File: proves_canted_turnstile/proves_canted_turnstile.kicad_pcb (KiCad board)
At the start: 2 copper layers, 11.2 x 10 mm, 17 parts, among them J1 Conn_Coaxial, U1 QBA-07+, U2 QBA-07+, U3 QBA-07+

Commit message: updates
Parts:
- UHF 180: renamed from UHF 0
- UHF 270: renamed from UHF 0
- UHF 90: renamed from UHF 0
- moved UHF 0 71.6 mm to (69.1, 108.8)
- moved UHF 180 71.6 mm to (62.4, 149.7)
- moved UHF 270 71.6 mm to (85.6, 131.4)
- moved UHF 90 71.6 mm to (30.9, 138.2)
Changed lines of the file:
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@@
 	(footprint "Turnstile_Library:Singular_Tape_Measure_Antenna"
 		(layer "F.Cu")
-		(at 121.746067 109.720487 50)
-		(property "Reference" "UHF 0"
+		(at 62.357 149.733 50)
+		(property "Reference" "UHF 180"
 			(at -4.967884 1.59847 0)
 			(unlocked yes)
@@
 	(footprint "Turnstile_Library:Singular_Tape_Measure_Antenna"
 		(layer "F.Cu")
-		(at 90.250067 98.163487 50)
-		(property "Reference" "UHF 0"
+		(at 30.861 138.176 50)
+		(property "Reference" "UHF 90"
 			(at -4.967884 1.59847 0)
 			(unlocked yes)
@@
 	(footprint "Turnstile_Library:Singular_Tape_Measure_Antenna"
 		(layer "F.Cu")
-		(at 144.987067 91.432487 50)
-		(property "Reference" "UHF 0"
+		(at 85.598 131.445 50)
+		(property "Reference" "UHF 270"
 			(at -4.967884 1.59847 0)
 			(unlocked yes)
@@
 	(footprint "Turnstile_Library:Singular_Tape_Measure_Antenna"
 		(layer "F.Cu")
-		(at 128.477067 68.826487 50)
+		(at 69.088 108.839 50)
 		(property "Reference" "UHF 0"
 			(at -4.967884 1.59847 0)

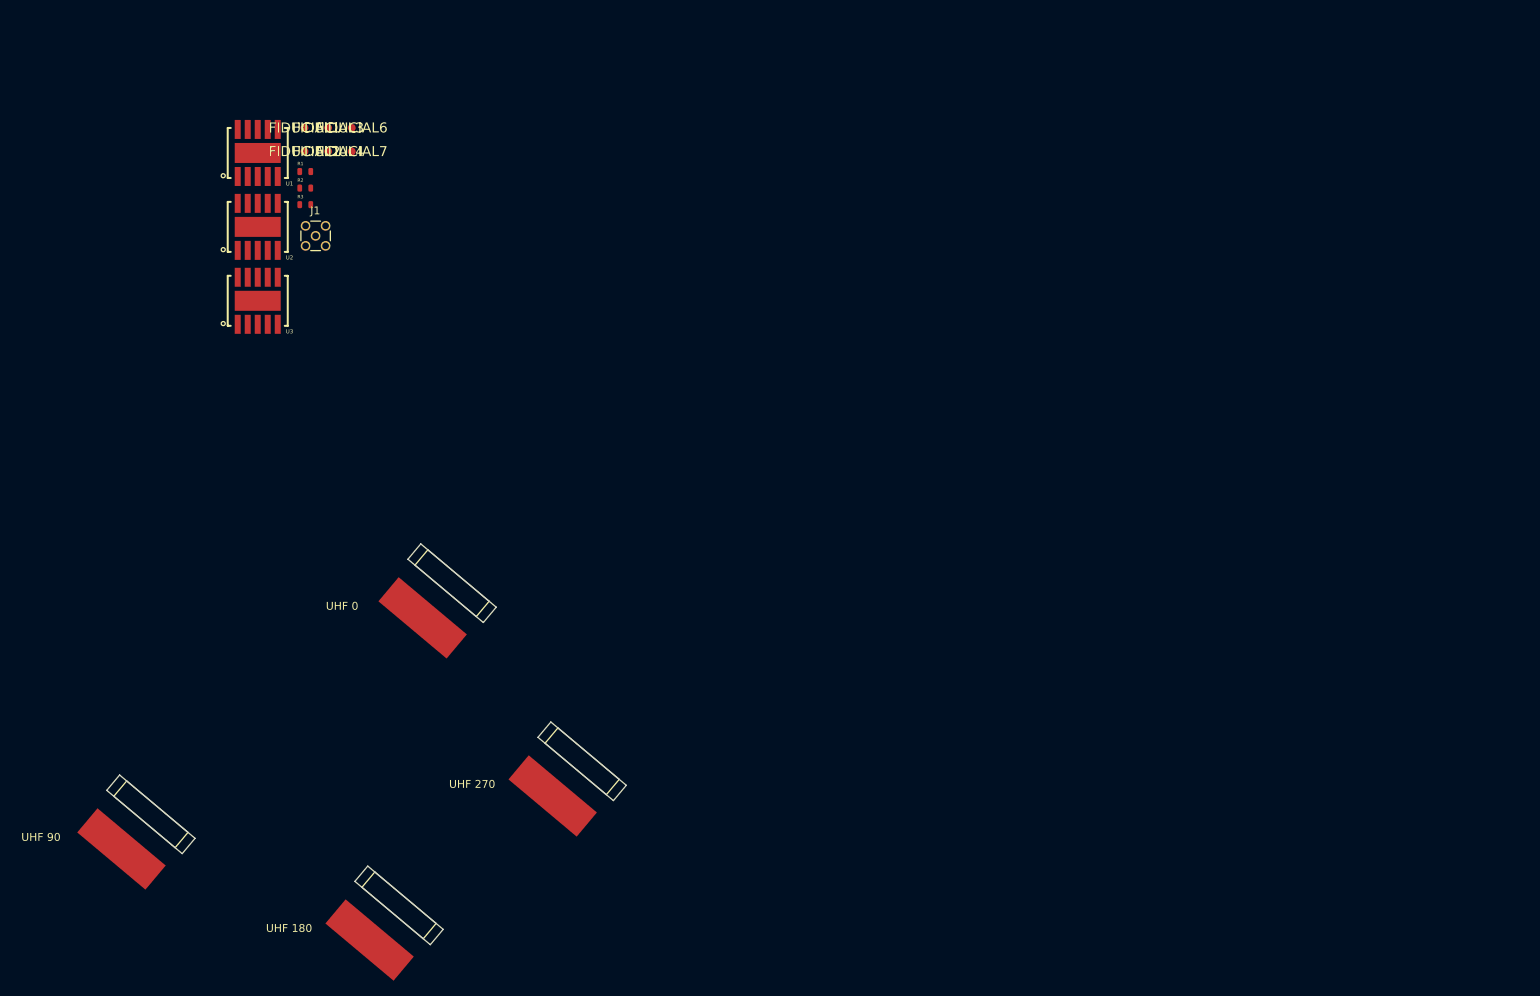
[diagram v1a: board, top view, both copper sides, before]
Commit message: made copper zones
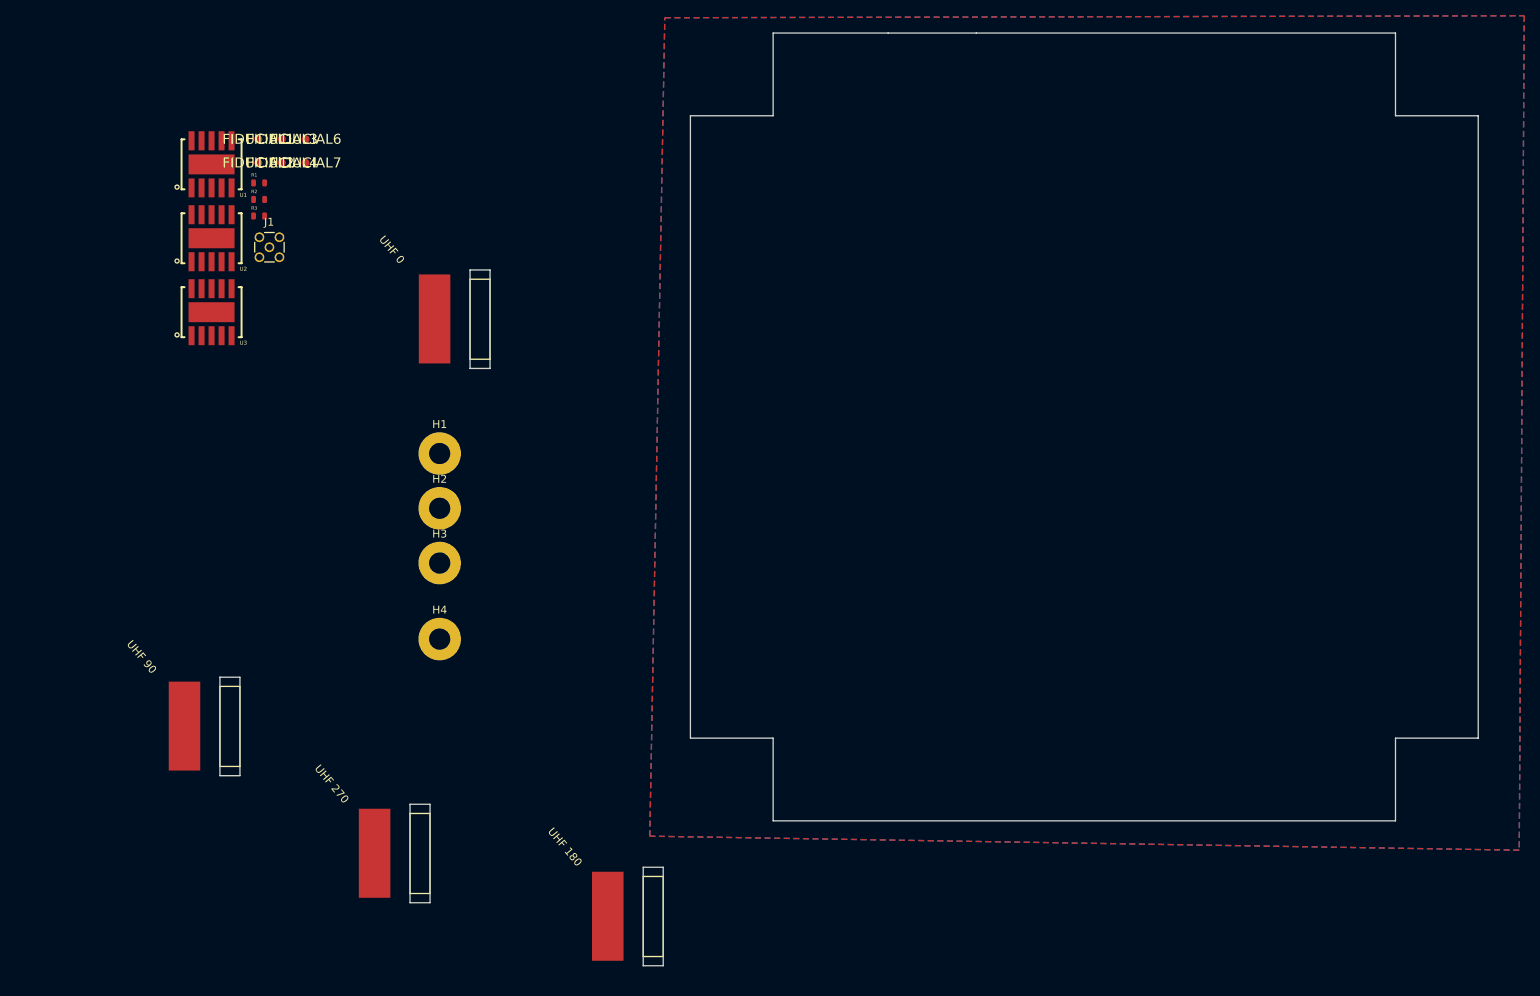
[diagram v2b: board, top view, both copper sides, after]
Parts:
- added H1: MountingHole, MountingHole:MountingHole_2.7mm_M2.5_Pad, F.Cu at (79.5, 94.3)
- added H2: MountingHole, MountingHole:MountingHole_2.7mm_M2.5_Pad, F.Cu at (79.5, 101.3)
- added H3: MountingHole, MountingHole:MountingHole_2.7mm_M2.5_Pad, F.Cu at (79.5, 108.2)
- added H4: MountingHole, MountingHole:MountingHole_2.7mm_M2.5_Pad, F.Cu at (79.5, 117.9)
- moved UHF 0 43.0 mm to (78.4, 66.8), turned to 0 degrees
- moved UHF 180 38.7 mm to (100.4, 142.6), turned to 0 degrees
- moved UHF 90 25.2 mm to (46.6, 118.5), turned to 0 degrees
- moved UHF 270 15.2 mm to (70.8, 134.7), turned to 0 degrees
- moved J1 6.04 mm to (57.9, 68.1)
- moved U2 6.04 mm to (50.5, 67.0)
- moved FIDUCIAL1 6.04 mm to (56.5, 54.4)
- moved FIDUCIAL2 6.04 mm to (56.5, 57.4)
- moved FIDUCIAL3 6.04 mm to (59.5, 54.4)
- moved FIDUCIAL4 6.04 mm to (59.5, 57.4)
- moved FIDUCIAL6 6.04 mm to (62.5, 54.4)
- moved FIDUCIAL7 6.04 mm to (62.5, 57.4)
- moved R1 6.04 mm to (56.6, 60.0)
- moved R2 6.04 mm to (56.6, 62.1)
- moved R3 6.04 mm to (56.6, 64.2)
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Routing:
- added copper zone on B.Cu, net GND
- added copper zone on F.Cu, net GND
- added copper zone on In1.Cu, net GND
- added copper zone on In2.Cu, net GND
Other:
- board size 11.2 x 10 mm -> 100 x 100 mm
- copper layers 2 -> 4
